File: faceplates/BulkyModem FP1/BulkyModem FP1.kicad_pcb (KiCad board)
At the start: 2 copper layers, 100 x 23.2 mm, 5 parts, among them M1 Mounting_Pin, M2 Mounting_Pin, M3 Mounting_Pin, M4 Mounting_Pin

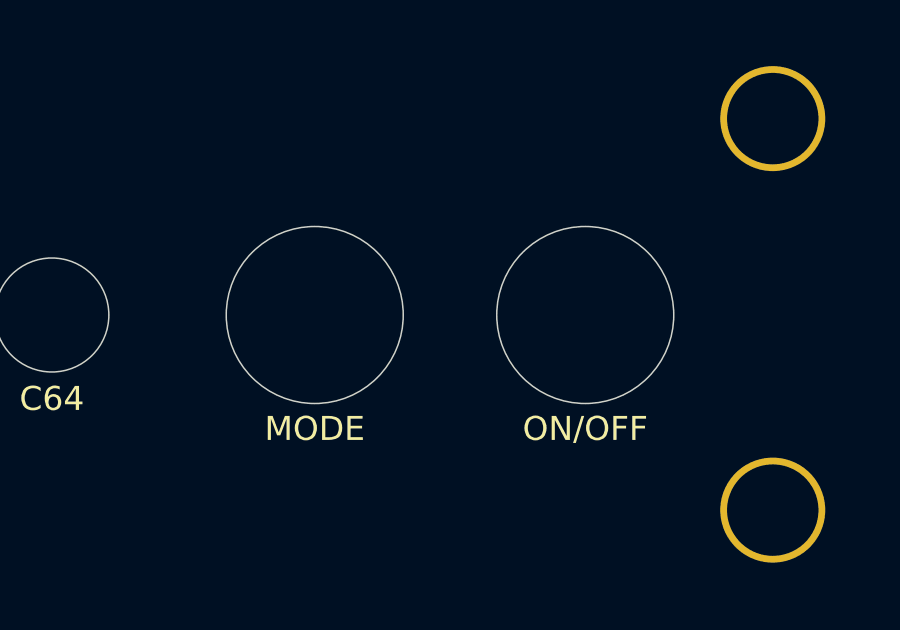
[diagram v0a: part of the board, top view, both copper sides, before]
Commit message: Slightly larger space for keycap
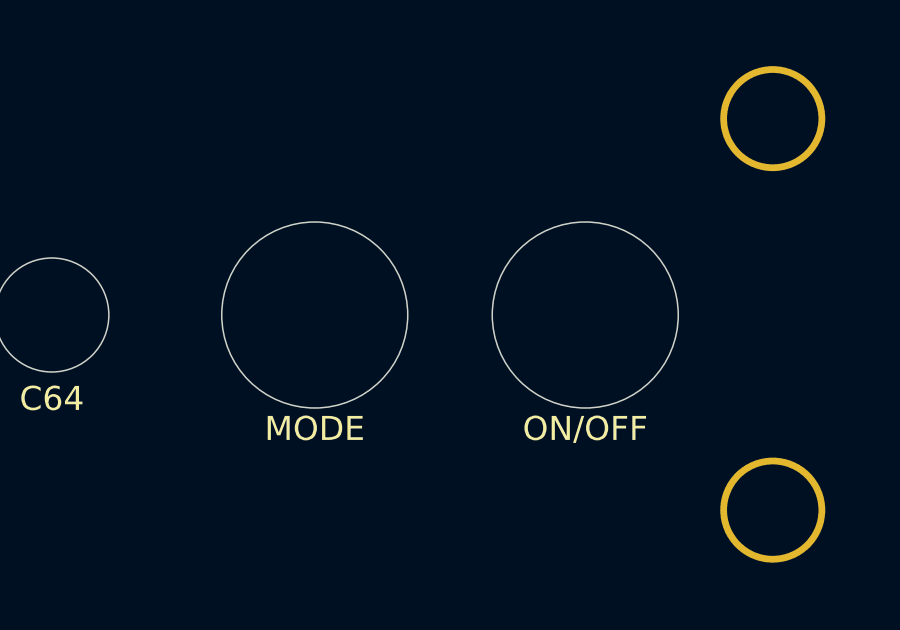
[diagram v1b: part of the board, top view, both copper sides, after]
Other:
- outline, holes or cut-outs redrawn
- board text added: "BulkyModem Front Panel FP1 (rev. B) github.com/tebl"
- board text removed: "BulkyModem Front Panel FP1 (rev. A) github.com/tebl"

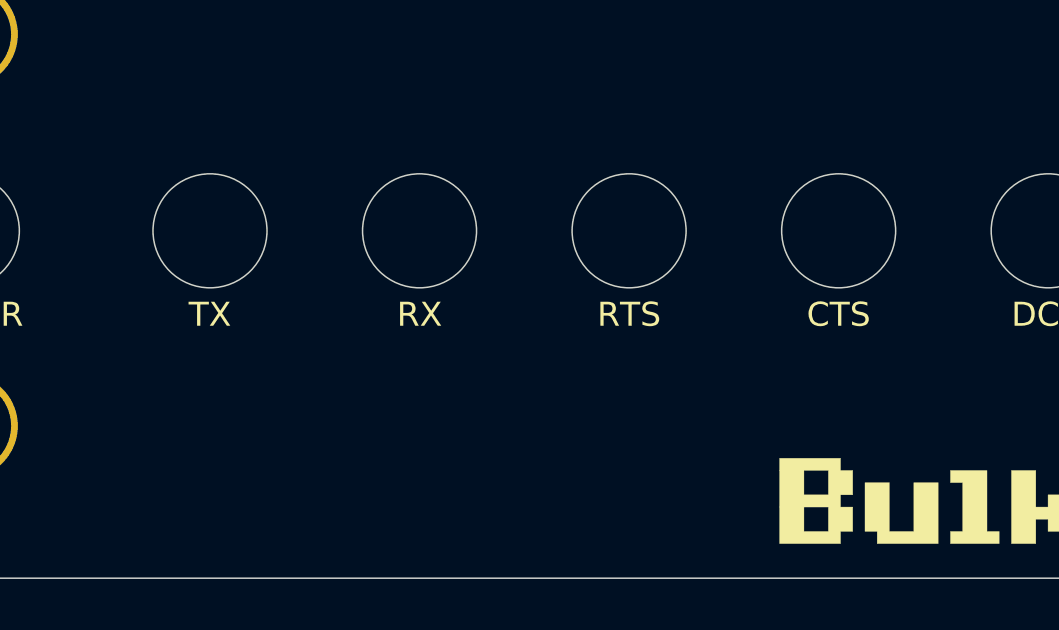
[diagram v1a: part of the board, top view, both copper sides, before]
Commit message: Revised version. Mainly buffering signals
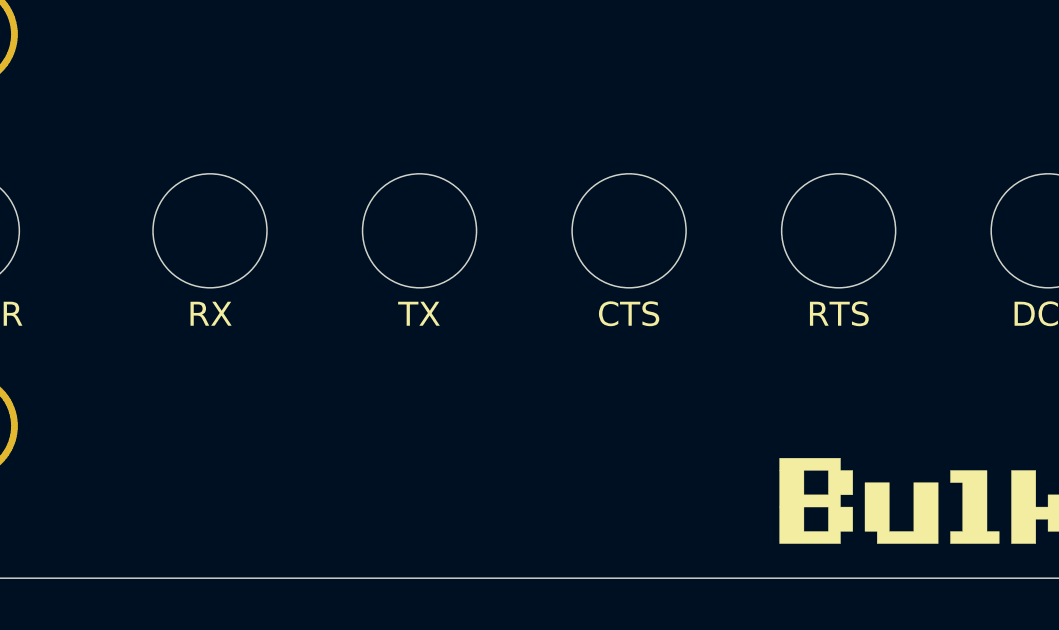
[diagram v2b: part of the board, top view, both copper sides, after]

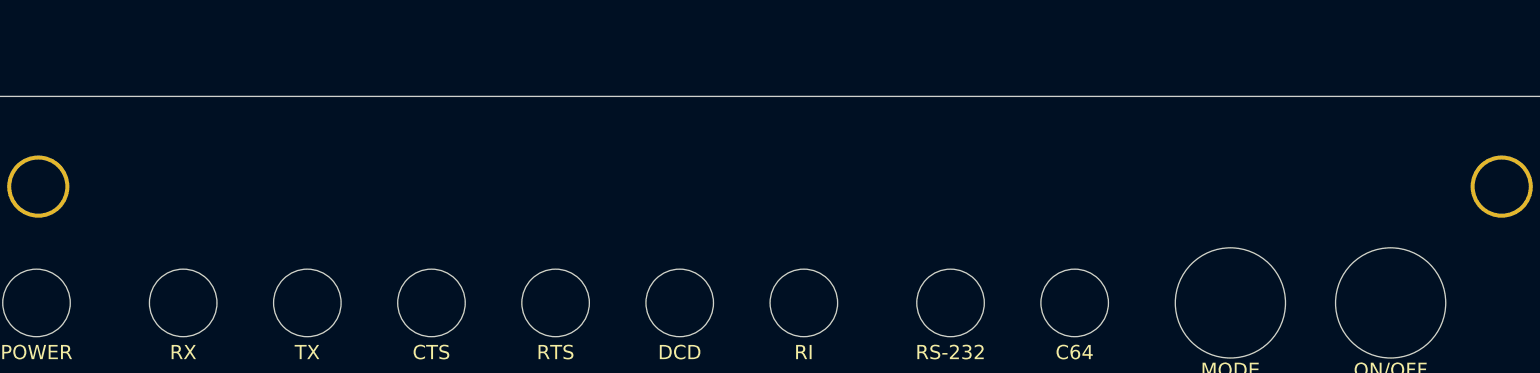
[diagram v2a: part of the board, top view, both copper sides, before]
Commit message: Accidentally lost top label
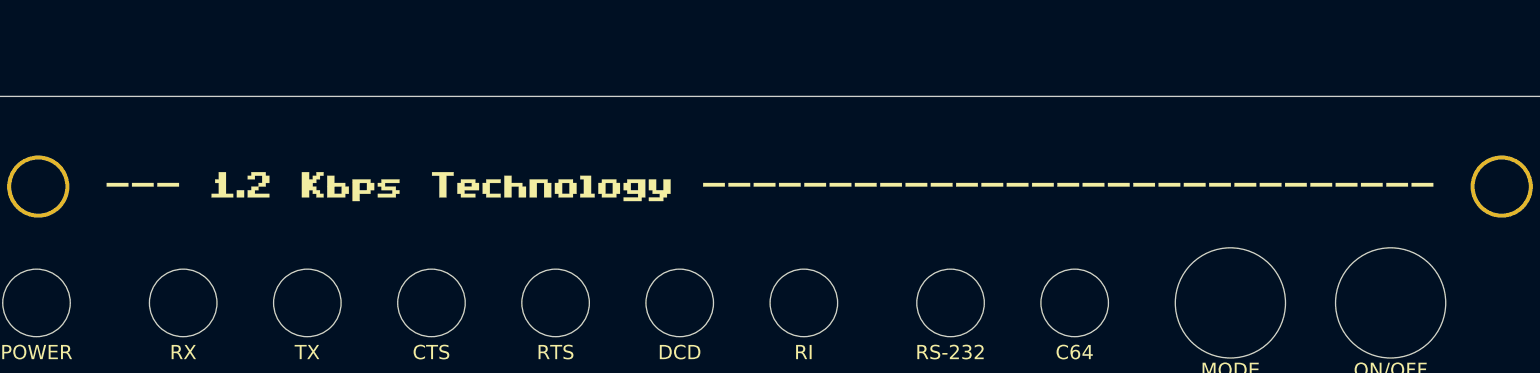
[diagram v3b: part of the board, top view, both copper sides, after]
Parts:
- added G***: LOGO, artwork:BulkyModem_robotics, F.Cu at (141.1, 116.0)
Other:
- net class Default removed
- net class PWR removed

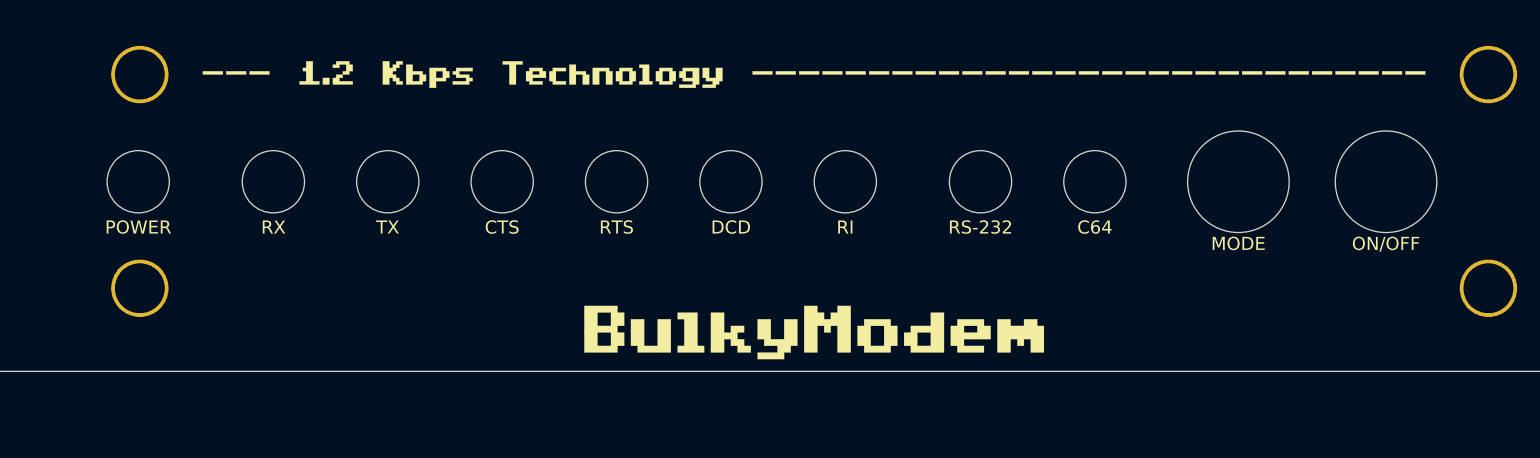
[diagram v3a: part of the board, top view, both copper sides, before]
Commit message: Changed FP1 labels to match FP2
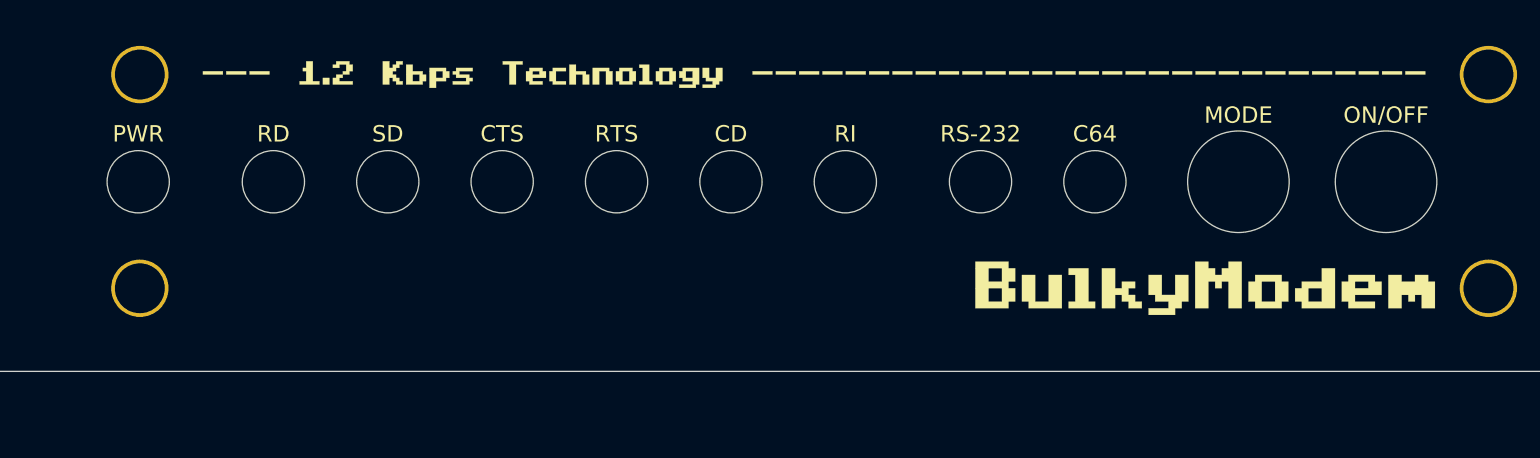
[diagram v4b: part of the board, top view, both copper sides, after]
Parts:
- moved G*** 24.0 mm to (165.0, 129.1)
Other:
- board text added: "CD"
- board text added: "PWR"
- board text added: "RD"
- board text added: "SD"
- board text removed: "DCD"
- board text removed: "POWER"
- board text removed: "RX"
- board text removed: "TX"
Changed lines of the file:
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@@
 		(locked yes)
 		(layer "F.Cu")
-		(at 141.09 131.8025)
+		(at 164.966 129.099)
 		(property "Reference" "G***"
 			(at 0 0 0)
@@
 		)
 	)
-	(gr_text "MODE"
-		(at 166.998 126.389 0)
+	(gr_text "PWR"
+		(at 99.815 119.674 0)
 		(layer "F.SilkS")
 		(effects
 			(font
-				(size 0.8 0.8)
-				(thickness 0.1)
-			)
-		)
-	)
-	(gr_text "RS-232"
-		(at 151.25 125.389 0)
+				(size 1 1)
+				(thickness 0.15)
+			)
+		)
+	)
+	(gr_text "CTS"
+		(at 122.04 119.674 0)
 		(layer "F.SilkS")
 		(effects
 			(font
-				(size 0.8 0.8)
-				(thickness 0.1)
-			)
-		)
-	)
-	(gr_text "POWER"
-		(at 99.815 125.389 0)
+				(size 1 1)
+				(thickness 0.15)
+			)
+		)
+	)
+	(gr_text "RS-232"
+		(at 151.25 119.674 0)
 		(layer "F.SilkS")
 		(effects
 			(font
-				(size 0.8 0.8)
-				(thickness 0.1)
-			)
-		)
-	)
-	(gr_text "RX"
-		(at 108.07 125.389 0)
+				(size 1 1)
+				(thickness 0.15)
+			)
+		)
+	)
+	(gr_text "RD"
+		(at 108.07 119.674 0)
 		(layer "F.SilkS")
 		(effects
 			(font
-				(size 0.8 0.8)
-				(thickness 0.1)
-			)
-		)
-	)
-	(gr_text "RTS"
-		(at 129.025 125.389 0)
+				(size 1 1)
+				(thickness 0.15)
+			)
+		)
+	)
+	(gr_text "CD"
+		(at 136.01 119.674 0)
 		(layer "F.SilkS")
 		(effects
 			(font
-				(size 0.8 0.8)
-				(thickness 0.1)
-			)
-		)
-	)
-	(gr_text "DCD"
-		(at 136.01 125.389 0)
+				(size 1 1)
+				(thickness 0.15)
+			)
+		)
+	)
+	(gr_text "SD"
+		(at 115.055 119.674 0)
 		(layer "F.SilkS")
 		(effects
 			(font
-				(size 0.8 0.8)
-				(thickness 0.1)
-			)
-		)
-	)
-	(gr_text "TX"
-		(at 115.055 125.389 0)
+				(size 1 1)
+				(thickness 0.15)
+			)
+		)
+	)
+	(gr_text "MODE"
+		(at 166.998 118.531 0)
 		(layer "F.SilkS")
 		(effects
 			(font
-				(size 0.8 0.8)
-				(thickness 0.1)
-			)
-		)
-	)
-	(gr_text "CTS"
-		(at 122.04 125.389 0)
+				(size 1 1)
+				(thickness 0.15)
+			)
+		)
+	)
+	(gr_text "ON/OFF"
+		(at 176.015 118.531 0)
 		(layer "F.SilkS")
 		(effects
 			(font
-				(size 0.8 0.8)
-				(thickness 0.1)
-			)
-		)
-	)
-	(gr_text "C64"
-		(at 158.235 125.389 0)
+				(size 1 1)
+				(thickness 0.15)
+			)
+		)
+	)
+	(gr_text "RTS"
+		(at 129.025 119.674 0)
 		(layer "F.SilkS")
 		(effects
 			(font
-				(size 0.8 0.8)
-				(thickness 0.1)
-			)
-		)
-	)
-	(gr_text "ON/OFF"
-		(at 176.015 126.389 0)
+				(size 1 1)
+				(thickness 0.15)
+			)
+		)
+	)
+	(gr_text "C64"
+		(at 158.235 119.674 0)
 		(layer "F.SilkS")
 		(effects
 			(font
-				(size 0.8 0.8)
-				(thickness 0.1)
+				(size 1 1)
+				(thickness 0.15)
 			)
 		)
 	)
 	(gr_text "RI"
-		(at 142.995 125.389 0)
+		(at 142.995 119.674 0)
 		(layer "F.SilkS")
 		(effects
 			(font
-				(size 0.8 0.8)
-				(thickness 0.1)
-			)
-		)
+				(size 1 1)
+				(thickness 0.15)
+			)
+		)
